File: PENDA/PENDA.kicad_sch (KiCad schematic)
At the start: 46 parts, among them J1 Alim 9v, J2 Jack MIDI, J3 In, J4 Out, J5 Carte SD, J6 Switch 1, J7 Switch 2, SW1 Param 1, SW2 Param 2, SW3 Param 3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

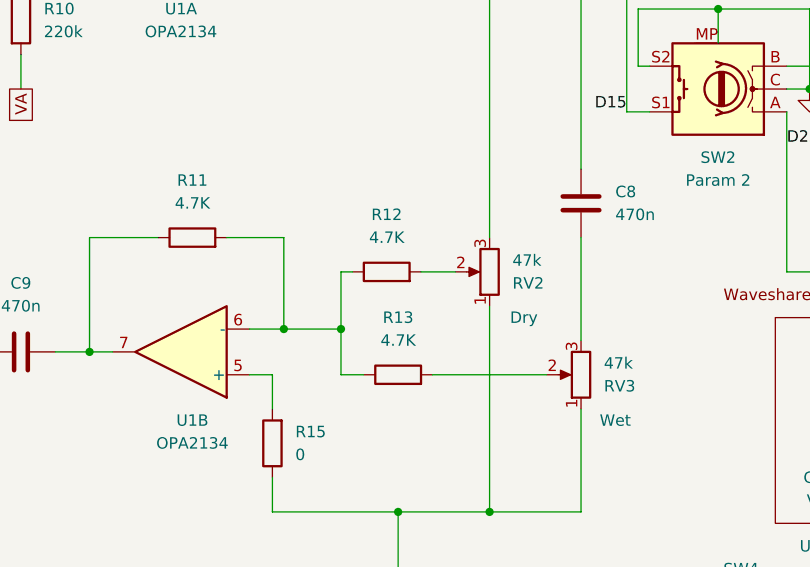
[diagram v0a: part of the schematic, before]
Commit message: Resistor and Potentiometer Value Update
Adjusted the values of resistors and potentiometers in the output summator circuit to enhance performance and functionality.
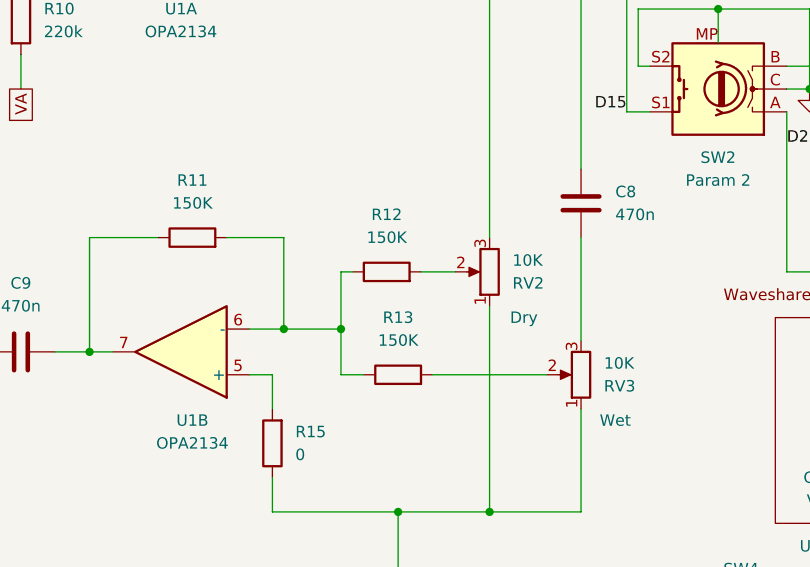
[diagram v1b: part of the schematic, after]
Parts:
- R11, R12, R13: value 4.7K -> 150K
- RV2, RV3: value 47k -> 10K
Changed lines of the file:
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@@
 			)
 		)
-		(property "Value" "4.7K"
+		(property "Value" "150K"
 			(at 81.28 121.92 90)
 			(effects
@@
 			)
 		)
-		(property "Value" "47k"
+		(property "Value" "10K"
 			(at 104.14 124.46 0)
 			(effects
@@
 			)
 		)
-		(property "Value" "4.7K"
+		(property "Value" "150K"
 			(at 80.01 110.49 90)
 			(effects
@@
 			)
 		)
-		(property "Value" "47k"
+		(property "Value" "10K"
 			(at 93.98 113.03 0)
 			(effects
@@
 			)
 		)
-		(property "Value" "4.7K"
+		(property "Value" "150K"
 			(at 58.42 106.68 90)
 			(effects
